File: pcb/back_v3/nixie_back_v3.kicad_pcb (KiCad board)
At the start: 2 copper layers, 110 x 50 mm, 26 parts, among them J1 UART, J2 BUTTONS, J3 LED, J4 POWER, J5 CONN_LEFT, J6 CONN_RIGHT, SW1 BOOT, SW2 RESET, U1 DS3231MZ, U2 ESP32-WROOM-E

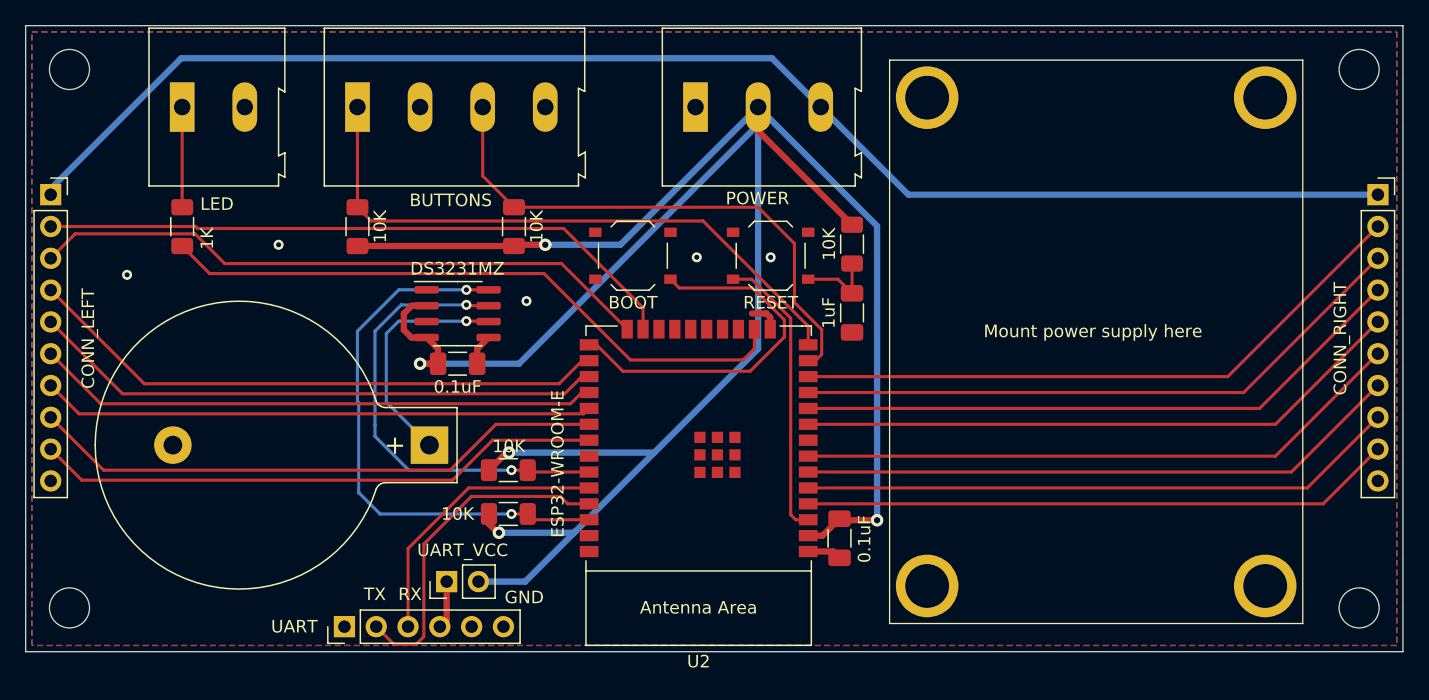
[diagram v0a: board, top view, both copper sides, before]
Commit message: Fix pin assignment on v3 back pcb
GPIO pins 34-39 on ESP32 are input only.
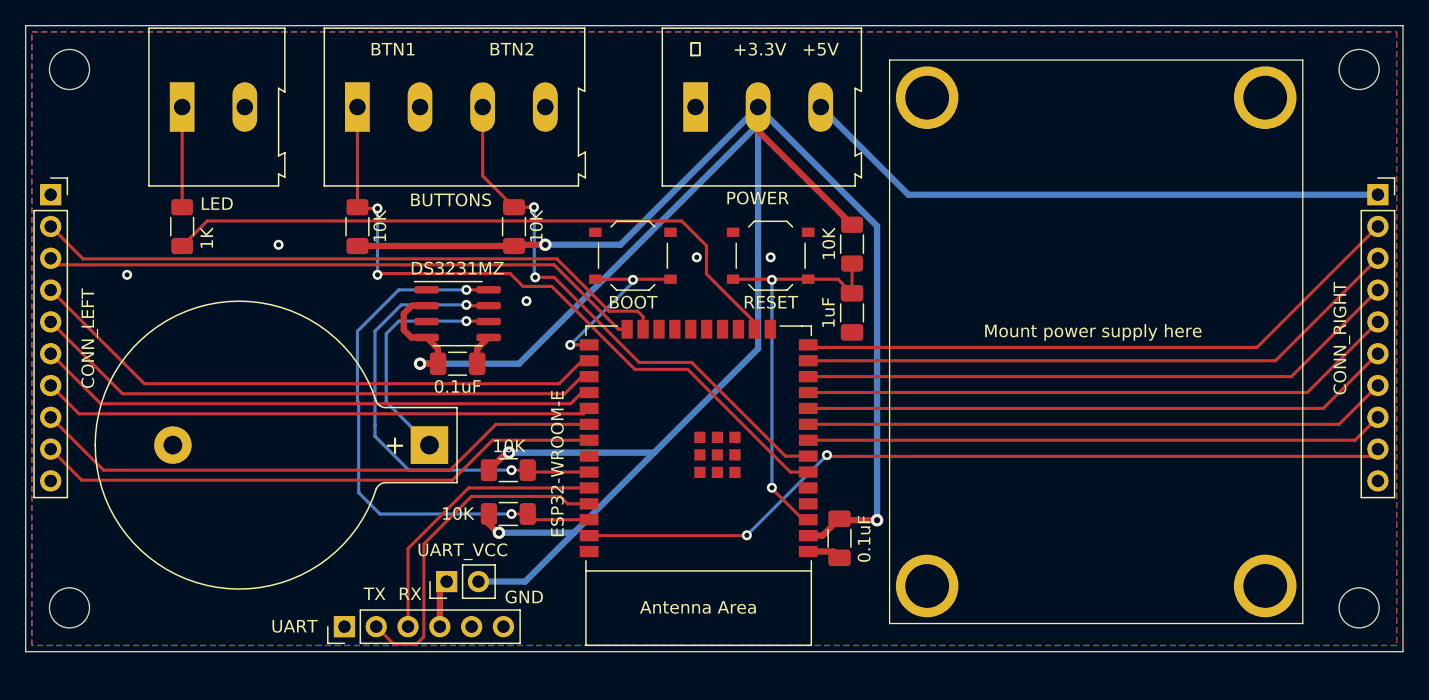
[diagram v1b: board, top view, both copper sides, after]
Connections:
- J5 pad 1: +5V -> unconnected-(J5-Pin_1-Pad1)
- U2 pad 10: /TUBE3C -> /TUBE4A
- U2 pad 11: /TUBE3B -> /TUBE3D
- U2 pad 12: /TUBE3A -> /TUBE3C
- U2 pad 13: /BTN2 -> /TUBE3B
- U2 pad 14: /BTN1 -> /TUBE3A
- U2 pad 37: unconnected-(U2-GPIO23-Pad37) -> /TUBE4D
- U2 pad 4: /TUBE4D -> unconnected-(U2-SENSOR_VP/GPIO36/ADC1_CH0-Pad4)
- U2 pad 5: /TUBE4C -> unconnected-(U2-SENSOR_VN/GPIO39/ADC1_CH3-Pad5)
- U2 pad 6: /TUBE4B -> /BTN1
- U2 pad 7: /TUBE4A -> /BTN2
- U2 pad 8: unconnected-(U2-32K_XP/GPIO32/ADC1_CH4-Pad8) -> /TUBE4C
- U2 pad 9: /TUBE3D -> /TUBE4B
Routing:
- net +5V: track 115.3 -> 47.4 mm
- net /TUBE4D: track 47.3 -> 65.9 mm, vias 0 -> 2
- net /BOOT: track 29.4 -> 14.8 mm, vias 0 -> 2
- net /BTN1: track 49.4 -> 55.9 mm, vias 0 -> 2
- net /RESET: track 29.5 -> 33.0 mm, vias 0 -> 2
- net GND: track 7.71 -> 5.18 mm
- net /TUBE1B: track 50.0 -> 48.4 mm
- net /TUBE4C: track 47.8 -> 46.3 mm
- net /TUBE4B: track 48.4 -> 46.8 mm
- net /TUBE4A: track 48.9 -> 47.3 mm
- net /TUBE3D: track 48.9 -> 47.8 mm
- net /TUBE3B: track 49.9 -> 48.9 mm
- net /TUBE3C: track 49.4 -> 48.4 mm
- net /TUBE3A: track 50.5 -> 49.6 mm
- net /UART_VCC: track 4.60 -> 3.83 mm
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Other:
- board text added: "+3.3V"
- board text added: "+5V"
- board text added: "BTN1"
- board text added: "BTN2"
- board text added: "Nixie Clock Back Panel v3.1 Ilya Strukov, 2023"
- board text added: "⏚"
- board text removed: "Nixie Clock Back Panel v3.0 Ilya Strukov, 2023"

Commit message: Misc PCB changes
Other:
- board text added: "+ -"
- board text added: "+HV ⏚ +3.3V ⏚ +5V ⏚"
- board text added: "VIN ⏚"
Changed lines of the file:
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@@
   (gr_rect (start 50 50) (end 160 100)
     (stroke (width 0.1) (type default)) (fill none) (layer "Edge.Cuts"))
-  (gr_text "This side towards front panel" (at 116 87) (layer "B.SilkS")
+  (gr_text "This side towards front panel" (at 143 84) (layer "B.SilkS")
     (effects (font (size 1 1) (thickness 0.15)) (justify left bottom mirror))
   )
-  (gr_text "Nixie Clock Back Panel v3.1\nIlya Strukov, 2023" (at 105 68) (layer "B.SilkS")
+  (gr_text "Nixie Clock Back Panel v3.1\nIlya Strukov, 2023" (at 132 71) (layer "B.SilkS")
     (effects (font (size 2 2) (thickness 0.3)) (justify bottom mirror))
   )
   (gr_text "Mount power supply here" (at 126.5 75) (layer "F.SilkS")
+    (effects (font (size 1 1) (thickness 0.15)) (justify left bottom))
+  )
+  (gr_text "+HV  ⏚  +3.3V ⏚  +5V  ⏚" (at 124.5 52.25) (layer "F.SilkS")
     (effects (font (size 1 1) (thickness 0.15)) (justify left bottom))
   )
@@
     (effects (font (size 1 1) (thickness 0.15)) (justify left bottom))
   )
+  (gr_text "VIN ⏚" (at 133.5 99.5) (layer "F.SilkS")
+    (effects (font (size 1 1) (thickness 0.15)) (justify left bottom))
+  )
   (gr_text "GND" (at 88.25 96.25) (layer "F.SilkS")
     (effects (font (size 1 1) (thickness 0.15)) (justify left bottom))
@@
     (effects (font (size 1 1) (thickness 0.15)) (justify left bottom))
   )
+  (gr_text "+  -" (at 63 52) (layer "F.SilkS")
+    (effects (font (size 1 1) (thickness 0.15)) (justify left bottom))
+  )
